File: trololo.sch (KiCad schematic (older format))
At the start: 96 parts, among them J1 USB_OTG, J10 Conn_02x12_Odd_Even, J11 Conn_02x02_Odd_Even, J12 PROTO1, J13 PROTO1, J14 PROTO1, J15 PROTO1, J16 PROTO1, J17 PROTO1, J18 PROTO1, J19 PROTO1, J2 USB_OTG, J3 Wuerth_7499010121A, J4 Micro_SD_Card, J5 Screw_Terminal_01x06, J6 Conn_02x12_Odd_Even, J7 USB_OTG, J8 Screw_Terminal_01x02, J9 Conn_02x12_Odd_Even, SW1 RESET, SW2 RESET, U1 STM32H743VITx, U10 USBLC6-2SC6, U2 KSZ8081RNA, U3 TCAN332DCNR, U4 ST485EBDR, U5 W25Q32JVZP, U6 APE1707H-33-HF, U7 USBLC6-2SC6, U8 STM32F042G6Ux, U9 USBLC6-2SC6, Y1 8MHz, Y2 32.768KHz, Y3 25MHz

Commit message: Final aproach with no can/485 isolation
Signed-off-by: Martin Ribelotta <martinribelotta@gmail.com>
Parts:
- added D10: NUP2105L, Package_TO_SOT_SMD:SOT-23, symbol Power_Protection:NUP2105L
- added D9: D_TVS, Diode_SMD:D_SMA, symbol Device:D_TVS
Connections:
- net GND: now also D10.3 (A)
- net RS485_A: now also D10.2 (K), D9.2 (A2)
- net RS485_B: now also D10.1 (K), D9.1 (A1)
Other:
- moved on the sheet: C1, C10, C11, C12, C13, C14, C15, C16, C17, C18, C19, C2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

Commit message: First isolation aproach
Signed-off-by: Martin Ribelotta <martinribelotta@gmail.com>
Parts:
- removed J12, J14, J15, J16, J17, J19: PROTO1, Connector_PinHeader_2.54mm:PinHeader_2x10_P2.54mm_Vertical, symbol Connector_Generic:Conn_02x10_Odd_Even
- removed U3: TCAN332DCNR, Package_TO_SOT_SMD:SOT-23-8, symbol Interface_CAN_LIN:TCAN332
- removed U4: ST485EBDR, Package_SO:SOIC-8_3.9x4.9mm_P1.27mm, symbol Interface_UART:ST485EBDR
- added C36, C37, C38, C40: 0.1u, Capacitor_SMD:C_0805_2012Metric, symbol Device:C_Small
- added C39: 10u, Capacitor_SMD:C_0805_2012Metric, symbol Device:C_Small
- added D11, D12: B120-E3, Diode_SMD:D_SMA, symbol Diode:B120-E3
- added TR1: ADTT1-6, Transformer_SMD:Pulse_P0926NL, symbol Transformer:ADTT1-6
- added U11: SN6505, Package_TO_SOT_SMD:SOT-23-6, symbol SN6505:SN6505
- added U3: ISO1050DUB, Package_SO:SOP-8_6.62x9.15mm_P2.54mm, symbol Interface_CAN_LIN:ISO1050DUB
- added U4: ISO3082DW, Package_SO:SOIC-16W_7.5x10.3mm_P1.27mm, symbol Interface_UART:ISO3082DW
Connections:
- net +3V3: now also C38.1, TR1.2, U11.2 (Vcc), U3.1 (VCC1), U4.1 (Vcc1); no longer J18.10 (Pin_10), J18.12 (Pin_12), J18.14 (Pin_14), J18.16 (Pin_16), J18.18 (Pin_18), J18.2 (Pin_2), J18.20 (Pin_20), J18.4 (Pin_4), J18.6 (Pin_6), J18.8 (Pin_8)
- net CAN_H: now also U3.7 (CANH)
- net CAN_L: now also U3.6 (CANL)
- net CAN_RX: now also U3.2 (RXD)
- net CAN_TX: now also U3.3 (TXD)
- net GND: now also C38.2, U11.4 (GND), U3.4 (GND1), U4.2 (GND1), U4.7 (GND1), U4.8 (GND1); no longer D1.3 (A), D10.3 (A), J5.2 (Pin_2), J5.5 (Pin_5)
- net RS485_A: now also U4.12 (A)
- net RS485_B: now also U4.13 (B)
- net RS485_DE: now also U4.4 (~RE), U4.6 (D)
- net RS485_RX: now also U4.3 (R)
- net RS485_TX: now also U4.5 (DE)
- net VDC: now also J18.10 (Pin_10), J18.12 (Pin_12), J18.14 (Pin_14), J18.16 (Pin_16), J18.18 (Pin_18), J18.2 (Pin_2), J18.20 (Pin_20), J18.4 (Pin_4), J18.6 (Pin_6), J18.8 (Pin_8)
- new net: TR1.3, U11.1 (D1)
- new net: TR1.1, U11.3 (D2)
- new net: D12.2 (A), TR1.4
- new net: D11.2 (A), TR1.6
- new net +5P: C36.1, C37.2, C39.1, C40.1, D11.1 (K), D12.1 (K), U3.8 (VCC2), U4.16 (Vcc2)
- new net GNDPWR: C36.2, C37.1, C39.2, C40.2, D1.3 (A), D10.3 (A), J5.2 (Pin_2), J5.5 (Pin_5), TR1.5, U3.5 (GND2), U4.10 (GND2), U4.15 (GND2), U4.9 (GND2)
- no-connect marks 121 -> 23
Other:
- note added: "COMM-PWR"
- moved on the sheet: C23, C24, D1, D10, D9

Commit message: Unknown changes
Signed-off-by: Martin Ribelotta <martinribelotta@gmail.com>
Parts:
- removed D3: D_Schottky_Small_ALT, Diode_SMD:D_SMA, symbol Device:D_Schottky_Small_ALT
- removed D9: D_TVS, Diode_SMD:D_SMA, symbol Device:D_TVS
- removed J1, J2, J7: USB_OTG, Connector_USB:USB_Micro-B_Molex_47346-0001, symbol Connector:USB_OTG
- removed J3: Wuerth_7499010121A, Connector_RJ:RJ45_Wuerth_7499010121A_Horizontal, symbol Connector:Wuerth_7499010121A
- removed U5: W25Q32JVZP, Package_SON:WSON-8-1EP_6x5mm_P1.27mm_EP3.4x4.3mm, symbol Memory_Flash:W25Q32JVZP
- removed U6: APE1707H-33-HF, Package_TO_SOT_SMD:TO-252-5_TabPin3, symbol Regulator_Switching:APE1707H-33-HF
- removed U8: STM32F042G6Ux, Package_DFN_QFN:QFN-28_4x4mm_P0.5mm, symbol MCU_ST_STM32F0:STM32F042G6Ux
- added J1, J2, J7: 10118194-0001LF, footprints:USB_Micro_B_Female_10118194-0001LF, symbol dk_USB-DVI-HDMI-Connectors:10118194-0001LF
- added J3: RJ45_Amphenol_RJMG1BD3B8K1ANR, Connector_RJ:RJ45_Amphenol_RJMG1BD3B8K1ANR, symbol Connector:RJ45_Amphenol_RJMG1BD3B8K1ANR
- added JP4, JP5: Jumper_2_Bridged, Jumper:SolderJumper-2_P1.3mm_Open_RoundedPad1.0x1.5mm, symbol Jumper:Jumper_2_Bridged
- added U12: TCAN332, Package_TO_SOT_SMD:SOT-23-8, symbol Interface_CAN_LIN:TCAN332
- added U13: ISL83483, Package_SO:SOIC-8_3.9x4.9mm_P1.27mm, symbol Interface_UART:ST485EBDR
- added U5: S25FL127SABMFI101, footprints:S25FL127SABMFI101, symbol 2019-03-05_02-01-41:S25FL127SABMFI101
- added U6: AP63203, Package_TO_SOT_SMD:TSOT-23-6, symbol reg_ap6320x:AP63203
- added U8: STM32F042F6Px, Package_SO:TSSOP-20_4.4x6.5mm_P0.65mm, symbol MCU_ST_STM32F0:STM32F042F4Px
- C1, C10, C11, C16, C2, C20, C21, C22, C23, C24, C25, C26, C27, C28, C3, C34, C35, C36, C37, C38, C4, C40, C6, C7, C8, C9: manf# (none) -> 885012207098
- C12, C13: manf# (none) -> CL21C180JBANNNC
- C14, C15: manf# (none) -> 885012007010
- C17: manf# (none) -> CL31B225KOHNNNE
- C18, C19, C5: manf# (none) -> LMK212B7475MG-T
- C29: value 470u -> 10u; footprint Capacitor_SMD:C_1206_3216Metric -> Capacitor_SMD:C_0805_2012Metric; manf# (none) -> CL21A106MQFNNNE
- C30: value 470u -> 2.2u; footprint Capacitor_SMD:C_1206_3216Metric -> Capacitor_SMD:C_0805_2012Metric; manf# (none) -> CL31B225KOHNNNE
- C31: value 0.1u -> 2.2u; manf# (none) -> CL31B225KOHNNNE
- C32, C33: manf# (none) -> 885012007012
- C39: manf# (none) -> CL21A106MQFNNNE
- D1, D10: manf# (none) -> NUP2105L
- D11, D12, D2, D4, D5, D6: manf# (none) -> B120-E3
- D7, D8: manf# (none) -> 150080RS75000
- J4: symbol Connector:Micro_SD_Card -> trololo-rescue:Micro_SD_Card-Connector; manf# (none) -> DM3D-SF
- J5: manf# (none) -> 1985234
- J8: manf# (none) -> 1985195
- L1: value L_Small -> 68uH; footprint Inductor_SMD:L_Bourns_SRN6045TA -> Inductor_SMD:L_6.3x6.3_H3; manf# (none) -> 1255AY-3R9N=P3
- R1, R11, R2, R5, R7: manf# (none) -> RC0805JR-074K7L
- R10, R8, R9: footprint Resistor_SMD:R_1806_4516Metric -> Resistor_SMD:R_0805_2012Metric; manf# (none) -> CRGCQ0805J22R
- R3, R4: footprint Resistor_SMD:R_1806_4516Metric -> Resistor_SMD:R_0805_2012Metric; manf# (none) -> RC0805JR-074K7L
- R6: manf# (none) -> RMCF0805FT6K49
- SW1: manf# (none) -> TL3342
- SW2: value RESET -> PC13; manf# (none) -> PTS645VM31-2 LFS
- TR1: manf# (none) -> 750315371
- U1: manf# (none) -> STM32H743VIT6
- U10, U7, U9: manf# (none) -> USBLC6-2SC6
- U11: manf# (none) -> SN6505BDBVR
- U2: manf# (none) -> KSZ8081RNA
- U3: symbol Interface_CAN_LIN:ISO1050DUB -> trololo-rescue:ISO1050DUB-Interface_CAN_LIN; manf# (none) -> ISO1050DUB
- U4: manf# (none) -> ISO3082DW
- Y1: manf# (none) -> NX5032GA-8MHZ-EXS00A-CG07039
- Y2: manf# (none) -> FC-135 32.7680KA-A5
- Y3: manf# (none) -> 445C33D25M00000
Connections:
- net +3V3: now also J13.1 (Pin_1), J13.11 (Pin_11), J13.13 (Pin_13), J13.15 (Pin_15), J13.17 (Pin_17), J13.19 (Pin_19), J13.3 (Pin_3), J13.5 (Pin_5), J13.7 (Pin_7), J13.9 (Pin_9), J6.22 (Pin_22), J6.24 (Pin_24), J9.2 (Pin_2), J9.4 (Pin_4), U11.5 (EN), JP5.2 (B), U12.3 (VCC), U13.8 (VCC), U5.8 (VCC), U6.1 (FB), U8.16 (VDD), U8.5 (VDDA); no longer C4.1, J18.1 (Pin_1), J18.11 (Pin_11), J18.13 (Pin_13), J18.15 (Pin_15), J18.17 (Pin_17), J18.19 (Pin_19), J18.3 (Pin_3), J18.5 (Pin_5), J18.7 (Pin_7), J18.9 (Pin_9), J6.2 (Pin_2), J6.4 (Pin_4), J6.6 (Pin_6), J9.1 (Pin_1), J9.3 (Pin_3), U1.6 (VBAT)
- net BOOT0_B: now also U8.1 (PB8)
- net CAN_H: now also U12.7 (CANH)
- net CAN_L: now also U12.6 (CANL)
- net CAN_RX: now also U12.4 (RXD)
- net CAN_TX: now also U12.1 (TXD)
- net C_USBD_D+: now also J1.3
- net C_USBD_D-: now also J1.2
- net C_USBH_D+: now also J2.3
- net C_USBH_D-: now also J2.2
- net C_USB_SER_D+: now also J7.3
- net C_USB_SER_D-: now also J7.2
- net GND: now also J10.11 (Pin_11), J10.13 (Pin_13), J10.15 (Pin_15), J10.17 (Pin_17), J10.19 (Pin_19), J10.21 (Pin_21), J10.3 (Pin_3), J10.5 (Pin_5), J10.7 (Pin_7), J10.9 (Pin_9), J18.1 (Pin_1), J18.11 (Pin_11), J18.13 (Pin_13), J18.15 (Pin_15), J18.17 (Pin_17), J18.19 (Pin_19), J18.3 (Pin_3), J18.5 (Pin_5), J18.7 (Pin_7), J18.9 (Pin_9), J6.21 (Pin_21), J6.23 (Pin_23), J9.1 (Pin_1), J1.5, J1.SH, J2.5, J2.SH, J3.13 (SHIELD), J3.L2 (LEDY_K), J3.L3 (LEDG_K), J3.R8 (GND), J7.5, J7.SH, JP4.1 (A), U12.2 (GND), U13.5 (GND), U5.4 (GND), U6.4 (GND), U8.15 (VSSA); no longer C28.2, J10.10 (Pin_10), J10.12 (Pin_12), J10.14 (Pin_14), J10.16 (Pin_16), J10.18 (Pin_18), J10.20 (Pin_20), J10.22 (Pin_22), J10.4 (Pin_4), J10.6 (Pin_6), J10.8 (Pin_8), J13.1 (Pin_1), J13.11 (Pin_11), J13.13 (Pin_13), J13.15 (Pin_15), J13.17 (Pin_17), J13.19 (Pin_19), J13.3 (Pin_3), J13.5 (Pin_5), J13.7 (Pin_7), J13.9 (Pin_9), J6.1 (Pin_1), J6.3 (Pin_3), J6.5 (Pin_5), J9.2 (Pin_2), J9.4 (Pin_4)
- net GNDPWR: now also JP4.2 (B)
- net PA0: now also J10.10 (Pin_10); no longer J10.9 (Pin_9)
- net PA15: now also J9.24 (Pin_24); no longer J9.23 (Pin_23)
- net PA3: now also J10.12 (Pin_12); no longer J10.11 (Pin_11)
- net PA4: now also J10.14 (Pin_14); no longer J10.13 (Pin_13)
- net PA5: now also J10.16 (Pin_16); no longer J10.15 (Pin_15)
- net PA6: now also J10.18 (Pin_18); no longer J10.17 (Pin_17)
- net PA8: now also J6.2 (Pin_2); no longer J6.24 (Pin_24)
- net PB0: now also J10.22 (Pin_22); no longer J10.21 (Pin_21)
- net PB1: now also J10.20 (Pin_20); no longer J10.19 (Pin_19)
- net PB10: now also J6.14 (Pin_14); no longer J6.12 (Pin_12)
- net PB3: now also J9.17 (Pin_17); no longer J9.18 (Pin_18)
- net PB4: now also J9.16 (Pin_16); no longer J9.15 (Pin_15)
- net PB5: now also J9.15 (Pin_15); no longer J9.16 (Pin_16)
- net PB6: now also J9.14 (Pin_14); no longer J9.13 (Pin_13)
- net PB7: now also J9.13 (Pin_13); no longer J9.14 (Pin_14)
- net PB8: now also J9.12 (Pin_12); no longer J9.11 (Pin_11)
- net PC0: now also J10.4 (Pin_4); no longer J10.3 (Pin_3)
- net PC10: now also J9.23 (Pin_23); no longer J9.24 (Pin_24)
- net PC13: now also J9.6 (Pin_6); no longer J9.5 (Pin_5)
- net PC2: now also J10.6 (Pin_6); no longer J10.5 (Pin_5)
- net PC3: now also J10.8 (Pin_8); no longer J10.7 (Pin_7)
- net PC6: now also J6.3 (Pin_3); no longer J6.21 (Pin_21)
- net PC7: now also J6.4 (Pin_4); no longer J6.22 (Pin_22)
- net PC9: now also J6.1 (Pin_1); no longer J6.23 (Pin_23)
- net PD10: now also J6.9 (Pin_9); no longer J6.15 (Pin_15)
- net PD11: now also J6.10 (Pin_10); no longer J6.16 (Pin_16)
- net PD12: now also J6.7 (Pin_7); no longer J6.17 (Pin_17)
- net PD13: now also J6.8 (Pin_8); no longer J6.18 (Pin_18)
- net PD14: now also J6.5 (Pin_5); no longer J6.19 (Pin_19)
- net PD15: now also J6.6 (Pin_6); no longer J6.20 (Pin_20)
- net PD3: now also J9.22 (Pin_22); no longer J9.21 (Pin_21)
- net PD4: now also J9.21 (Pin_21); no longer J9.22 (Pin_22)
- net PD5: now also J9.20 (Pin_20); no longer J9.19 (Pin_19)
- net PD6: now also J9.19 (Pin_19); no longer J9.20 (Pin_20)
- net PD7: now also J9.18 (Pin_18); no longer J9.17 (Pin_17)
- net PD8: now also J6.11 (Pin_11); no longer J6.13 (Pin_13)
- net PD9: now also J6.12 (Pin_12); no longer J6.14 (Pin_14)
- net PE11: now also J6.17 (Pin_17); no longer J6.7 (Pin_7)
- net PE12: now also J6.18 (Pin_18); no longer J6.8 (Pin_8)
- net PE13: now also J6.15 (Pin_15); no longer J6.9 (Pin_9)
- net PE14: now also J6.16 (Pin_16); no longer J6.10 (Pin_10)
- net PE15: now also J6.13 (Pin_13); no longer J6.11 (Pin_11)
- net PE2: now also J9.11 (Pin_11); no longer J9.12 (Pin_12)
- net PE3: now also J9.10 (Pin_10); no longer J9.9 (Pin_9)
- net PE4: now also J9.9 (Pin_9); no longer J9.10 (Pin_10)
- net PE5: now also J9.8 (Pin_8); no longer J9.7 (Pin_7)
- net PE6: now also J9.7 (Pin_7); no longer J9.8 (Pin_8)
- net QSPI_IO0: now also U5.5 (SI/IO0)
- net QSPI_IO1: now also U5.2 (SO/IO1)
- net QSPI_IO2: now also U5.3 (*WP/IO2)
- net QSPI_IO3: now also U5.7 (*HOLD/IO3)
- net QSPI_SCK: now also U5.6 (CLK)
- net RD+: now also J3.R3 (RD+)
- net RD-: now also J3.R6 (RD-)
- net RS485_A: now also U13.6 (A)
- net RS485_B: now also U13.7 (B)
- net RS485_DE: now also U13.2 (~RE), U13.3 (DE)
- net RS485_RX: now also U13.1 (RO)
- net RS485_TX: now also U13.4 (DI)
- net SWCLK: now also U8.6 (PA0)
- net SWCLK_B: now also U8.20 (PA14)
- net SWDIO: now also U8.7 (PA1)
- net SWDIO_B: now also U8.19 (PA13)
- net TD+: now also J3.R1 (TD+)
- net TD-: now also J3.R2 (TD-)
- net U1_RX: now also J6.19 (Pin_19)
- net U1_TX: now also J6.20 (Pin_20)
- net U2_RX: now also U8.9 (PA3)
- net U2_TX: now also U8.8 (PA2)
- net USB_SER_D+: now also U8.18 (PA10/PA12)
- net USB_SER_D-: now also U8.17 (PA9/PA11)
- net VBUS1: now also J1.1
- net VBUS2: now also J7.1
- net VBUS3: now also J2.1
- net VDC: now also U6.2 (EN), U6.3 (VIN); no longer C28.1
- net ~QSPI_CS: now also U5.1 (*CS)
- net ~RESET: now also J9.5 (Pin_5), U8.10 (PA4); no longer J9.6 (Pin_6)
- net at C34.2: now also J3.R4 (TCT)
- net at R8.1: now also J3.L1 (LEDY_A), J3.L4 (LEDG_A)
- net at C35.2: now also J3.R5 (RCT)
- net at C27.2: now also U8.4 (NRST)
- net at L1.1: now also C28.2, U6.5 (SW)
- new net: C28.1, U6.6 (BST)
- new net +BATT: C4.1, J9.3 (Pin_3), JP5.1 (A), U1.6 (VBAT)
- no-connect marks 23 -> 15
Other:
- note added: "COMM (non isolated version)\n- optional -"
- moved on the sheet: C25, C26, C27, C28, C30, C31, C34, C35, C4, C6, D2, D4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

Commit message: More unprecie modifications
The log messages on this git sucks

Signed-off-by: Martin Ribelotta <martinribelotta@gmail.com>
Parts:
- added J12: VBATJ, TestPoint:TestPoint_Loop_D1.80mm_Drill1.0mm_Beaded, symbol Connector:Conn_01x01_Female
- JP5: footprint Jumper:SolderJumper-2_P1.3mm_Open_RoundedPad1.0x1.5mm -> Jumper:SolderJumper-2_P1.3mm_Bridged_RoundedPad1.0x1.5mm
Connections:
- net +BATT: now also J12.1 (Pin_1)
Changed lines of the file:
@@
 	0    1    1    0
 $EndComp
-$Comp
-L Jumper:Jumper_2_Bridged JP5
-U 1 1 5CE929CB
-P 1100 4100
-F 0 "JP5" V 1050 4050 50  0000 R CNN
-F 1 "Jumper_2_Bridged" H 1450 4200 50  0000 R CNN
-F 2 "Jumper:SolderJumper-2_P1.3mm_Open_RoundedPad1.0x1.5mm" H 1100 4100 50  0001 C CNN
-F 3 "~" H 1100 4100 50  0001 C CNN
-	1    1100 4100
-	0    -1   -1   0
-$EndComp
+Connection ~ 1100 4500
 Wire Wire Line
 	1100 4300 1100 4500
-Connection ~ 1100 4500
 $Comp
 L power:+3.3V #PWR0184
@@
 	1    0    0    -1
 $EndComp
+$Comp
+L Jumper:Jumper_2_Bridged JP5
+U 1 1 5CE929CB
+P 1100 4100
+F 0 "JP5" V 1050 4050 50  0000 R CNN
+F 1 "Jumper_2_Bridged" H 1450 4200 50  0000 R CNN
+F 2 "Jumper:SolderJumper-2_P1.3mm_Bridged_RoundedPad1.0x1.5mm" H 1100 4100 50  0001 C CNN
+F 3 "~" H 1100 4100 50  0001 C CNN
+	1    1100 4100
+	0    -1   -1   0
+$EndComp
+$Comp
+L Connector:Conn_01x01_Female J12
+U 1 1 5CE79753
+P 1300 4500
+F 0 "J12" H 1328 4526 50  0000 L CNN
+F 1 "VBATJ" H 1328 4435 50  0000 L CNN
+F 2 "TestPoint:TestPoint_Loop_D1.80mm_Drill1.0mm_Beaded" H 1300 4500 50  0001 C CNN
+F 3 "~" H 1300 4500 50  0001 C CNN
+	1    1300 4500
+	1    0    0    -1
+$EndComp

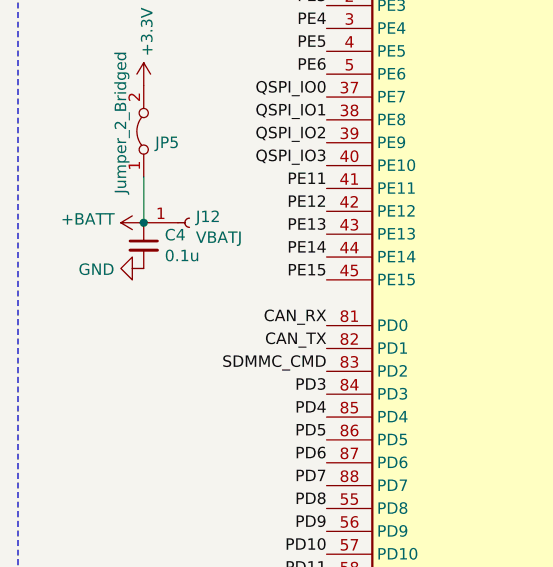
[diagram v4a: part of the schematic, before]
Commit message: Add battery pins
Signed-off-by: Martin Ribelotta <martinribelotta@gmail.com>
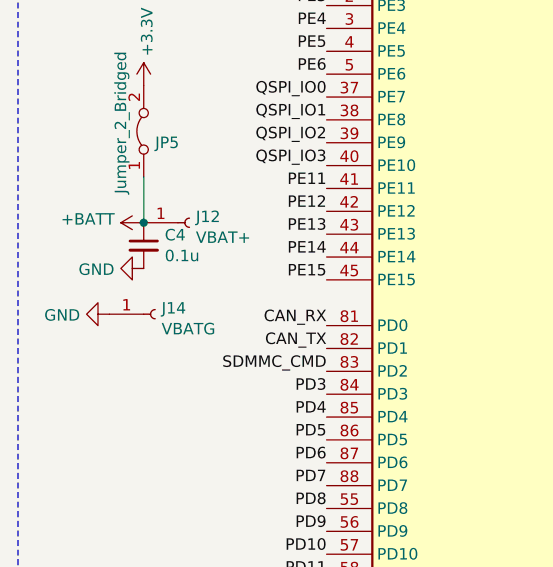
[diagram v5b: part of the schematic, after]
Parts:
- added J14: VBATG, TestPoint:TestPoint_Loop_D1.80mm_Drill1.0mm_Beaded, symbol Connector:Conn_01x01_Female
- J12: value VBATJ -> VBAT+
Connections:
- net GND: now also J14.1 (Pin_1)
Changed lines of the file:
@@
 encoding utf-8
 Sheet 1 1
-Title ""
+Title "DragonMAN"
 Date ""
-Rev ""
+Rev "0.1"
 Comp ""
 Comment1 ""
@@
 P 1300 4500
 F 0 "J12" H 1328 4526 50  0000 L CNN
-F 1 "VBATJ" H 1328 4435 50  0000 L CNN
+F 1 "VBAT+" H 1328 4435 50  0000 L CNN
 F 2 "TestPoint:TestPoint_Loop_D1.80mm_Drill1.0mm_Beaded" H 1300 4500 50  0001 C CNN
 F 3 "~" H 1300 4500 50  0001 C CNN
@@
 	1    0    0    -1
 $EndComp
+$Comp
+L Connector:Conn_01x01_Female J14
+U 1 1 5CEBA95D
+P 1150 4900
+F 0 "J14" H 1178 4926 50  0000 L CNN
+F 1 "VBATG" H 1178 4835 50  0000 L CNN
+F 2 "TestPoint:TestPoint_Loop_D1.80mm_Drill1.0mm_Beaded" H 1150 4900 50  0001 C CNN
+F 3 "~" H 1150 4900 50  0001 C CNN
+	1    1150 4900
+	1    0    0    -1
+$EndComp
+$Comp
+L power:GND #PWR04
+U 1 1 5CEBBA60
+P 950 4900
+F 0 "#PWR04" H 950 4650 50  0001 C CNN
+F 1 "GND" V 955 4772 50  0000 R CNN
+F 2 "" H 950 4900 50  0001 C CNN
+F 3 "" H 950 4900 50  0001 C CNN
+	1    950  4900
+	0    1    1    0
+$EndComp
 $EndSCHEMATC

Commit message: Add logos and change reset button and user led position
Signed-off-by: Martin Ribelotta <martinribelotta@gmail.com>
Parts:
- J4: symbol trololo-rescue:Micro_SD_Card-Connector -> trololo-rescue:Micro_SD_Card-Connector-trololo-rescue
- SW1: footprint Button_Switch_SMD:SW_SPST_TL3342 -> Buttons_Switches_THT:SW_Tactile_SPST_Angled_PTS645Vx31-2LFS
- SW2: footprint Button_Switch_THT:SW_Tactile_SPST_Angled_PTS645Vx31-2LFS -> Buttons_Switches_THT:SW_Tactile_SPST_Angled_PTS645Vx31-2LFS
- U11: symbol SN6505:SN6505 -> trololo-rescue:SN6505-SN6505
- U3: symbol trololo-rescue:ISO1050DUB-Interface_CAN_LIN -> trololo-rescue:ISO1050DUB-Interface_CAN_LIN-trololo-rescue
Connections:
- net GND: now also SW1.2; no longer SW1.1
- net ~RESET: now also SW1.1; no longer SW1.2
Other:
- moved on the sheet: SW1
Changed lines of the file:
@@
 NoConn ~ 5550 9700
 $Comp
-L trololo-rescue:Micro_SD_Card-Connector J4
+L trololo-rescue:Micro_SD_Card-Connector-trololo-rescue J4
 U 1 1 5C625641
 P 7050 1250
@@
 F 0 "SW1" V 8846 1252 50  0000 R CNN
 F 1 "RESET" V 8755 1252 50  0000 R CNN
-F 2 "Button_Switch_SMD:SW_SPST_TL3342" H 8800 1500 50  0001 C CNN
+F 2 "Buttons_Switches_THT:SW_Tactile_SPST_Angled_PTS645Vx31-2LFS" H 8800 1500 50  0001 C CNN
 F 3 "~" H 8800 1500 50  0001 C CNN
 F 4 "TL3342" H 0   0   50  0001 C CNN "manf#"
 	1    8800 1300
-	0    -1   -1   0
+	0    1    1    0
 $EndComp
 $Comp
@@
 F 0 "SW2" V 9296 1252 50  0000 R CNN
 F 1 "PC13" V 9205 1252 50  0000 R CNN
-F 2 "Button_Switch_THT:SW_Tactile_SPST_Angled_PTS645Vx31-2LFS" H 9250 1500 50  0001 C CNN
+F 2 "Buttons_Switches_THT:SW_Tactile_SPST_Angled_PTS645Vx31-2LFS" H 9250 1500 50  0001 C CNN
 F 3 "~" H 9250 1500 50  0001 C CNN
 F 4 "PTS645VM31-2 LFS" H 0   0   50  0001 C CNN "manf#"
@@
 	14950 5400 14950 5350
 $Comp
-L trololo-rescue:ISO1050DUB-Interface_CAN_LIN U3
+L trololo-rescue:ISO1050DUB-Interface_CAN_LIN-trololo-rescue U3
 U 1 1 5C76F366
 P 13550 3900
@@
 	12350 8350 12450 8350
 $Comp
-L SN6505:SN6505 U11
+L trololo-rescue:SN6505-SN6505 U11
 U 1 1 5CA512D2
 P 13400 6750

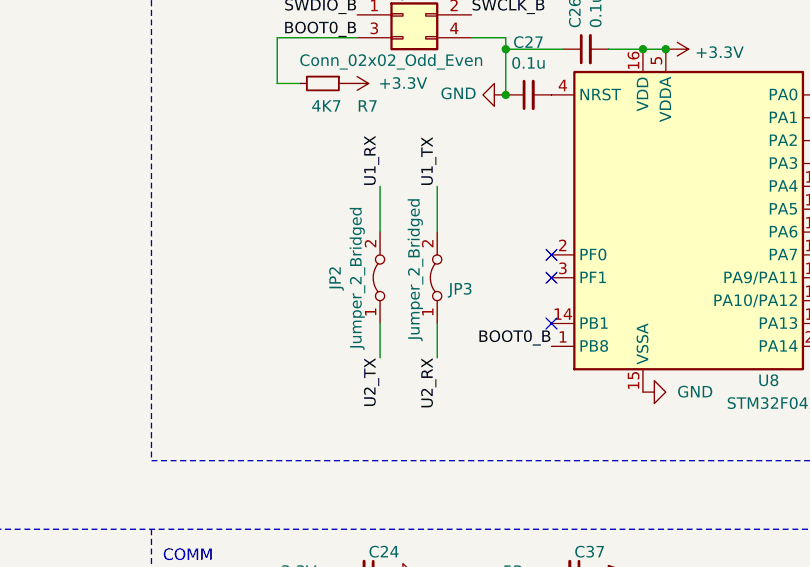
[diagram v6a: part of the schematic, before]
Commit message: Add patrocinator logo, silkscreen correctios and minor route changes
Signed-off-by: Martin Ribelotta <martinribelotta@gmail.com>
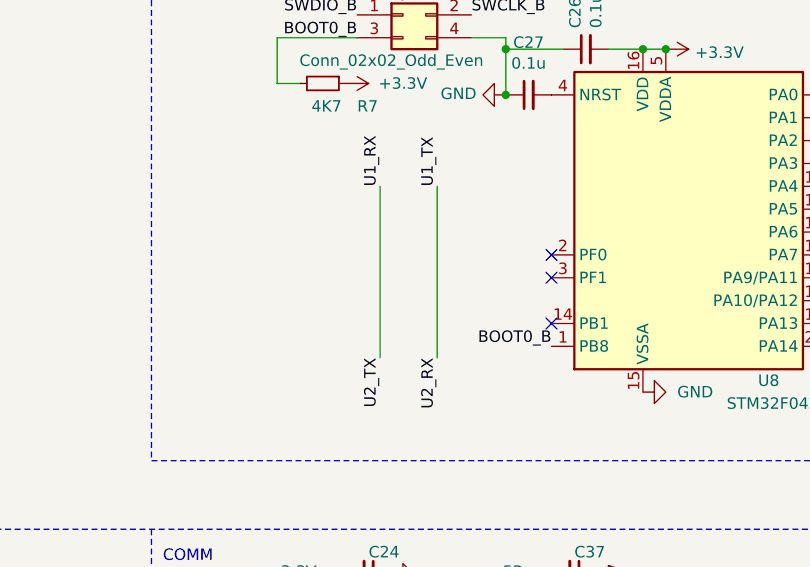
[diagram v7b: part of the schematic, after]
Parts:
- removed JP2, JP3: Jumper_2_Bridged, Jumper:SolderJumper-2_P1.3mm_Bridged_RoundedPad1.0x1.5mm, symbol Jumper:Jumper_2_Bridged
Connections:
- net U2_RX is gone; now on net U1_TX: U8.9 (PA3)
- net U2_TX is gone; now on net U1_RX: U8.8 (PA2)
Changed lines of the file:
@@
 	13850 1100 14100 1100
 Connection ~ 13850 1300
-$Comp
-L Jumper:Jumper_2_Bridged JP2
-U 1 1 5C769611
-P 13300 2100
-F 0 "JP2" H 13300 2295 50  0000 C CNN
-F 1 "Jumper_2_Bridged" H 13300 2204 50  0000 C CNN
-F 2 "Jumper:SolderJumper-2_P1.3mm_Bridged_RoundedPad1.0x1.5mm" H 13300 2100 50  0001 C CNN
-F 3 "~" H 13300 2100 50  0001 C CNN
-	1    13300 2100
-	0    -1   -1   0
-$EndComp
-Wire Wire Line
-	13300 1700 13300 1900
-$Comp
-L Jumper:Jumper_2_Bridged JP3
-U 1 1 5C77BEDA
-P 13550 2100
-F 0 "JP3" V 13500 2050 50  0000 R CNN
-F 1 "Jumper_2_Bridged" H 13900 2200 50  0000 R CNN
-F 2 "Jumper:SolderJumper-2_P1.3mm_Bridged_RoundedPad1.0x1.5mm" H 13550 2100 50  0001 C CNN
-F 3 "~" H 13550 2100 50  0001 C CNN
-	1    13550 2100
-	0    -1   -1   0
-$EndComp
-Wire Wire Line
-	13550 1700 13550 1900
-Wire Wire Line
-	13550 2300 13550 2450
-Wire Wire Line
-	13300 2450 13300 2300
 Text Label 13550 2450 3    50   ~ 0
 U2_RX
@@
 	0    1    1    0
 $EndComp
+Wire Wire Line
+	13300 1700 13300 2450
+Wire Wire Line
+	13550 1700 13550 2450
 $EndSCHEMATC
